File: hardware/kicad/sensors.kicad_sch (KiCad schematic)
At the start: 21 parts, among them J3 JST SM06B-GHS-TB (SEN66-SIN-T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, J4 1x5 P1.27mm through-hole head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, J7 1x8 P2.54 mm female socket (M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, J8 1x8 P2.54 mm female socket (M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

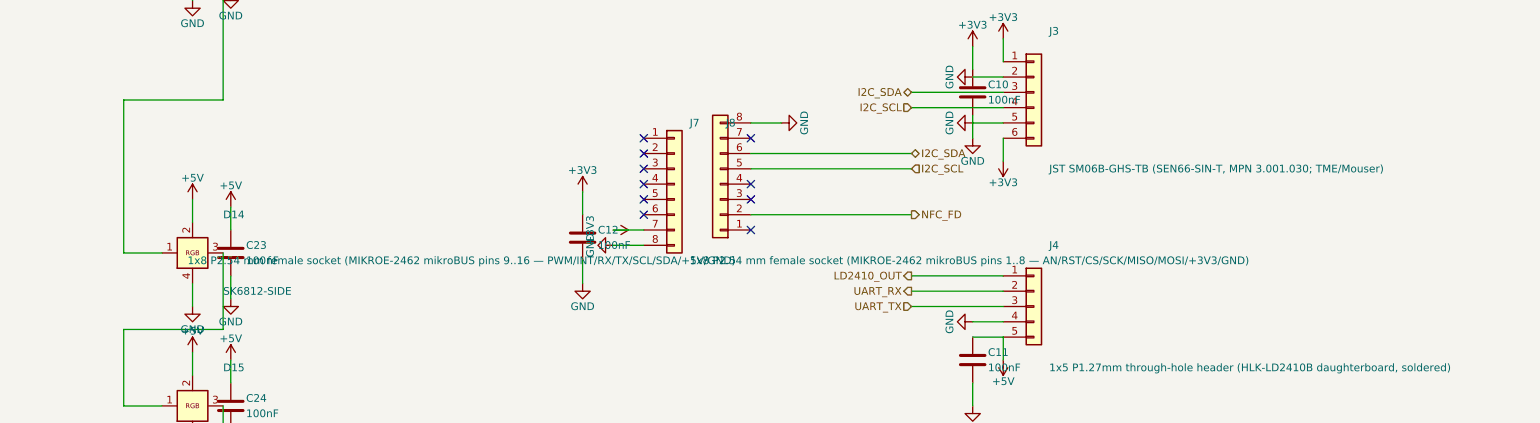
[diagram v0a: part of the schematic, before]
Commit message: hardware+firmware: remove the dynamic NFC tag (MIKROE-2462 / NT3H1101)
Closes #7.

The NFC feature is dropped entirely: RF coupling through the AK-N-94
cover is unusable as integrated, the only workable fix (cover-mounted
antenna) breaks the aesthetic pillar, and the LED ring + HA dashboard
already cover the need. Recorded in CLAUDE.md Out-of-scope.

Hardware (boardgen):
- MOD2 (oas:MIKROE-2462_Reference), J7 + J8 mikroBUS sockets and C12
  decoupling removed from schematic, placement, footprints, Z-clearance
  and the stage-18 whitelist (9 -> 8 documented customs).
- GPIO 3 (net NFC_FD) freed -> spare no_connect, same pattern as GPIO 1
  in the SW1 removal; ten spare safe-non-strap GPIOs now.
- Routing snapshot 600 seg + 40 via -> 586 seg + 43 via: /MCU/NFC_FD
  (2 seg) and 12 dead GND stitches anchored at the removed pads swept;
  3 bridge vias added where former J7.7/J8.5/J8.6 THT pads carried the
  live +3V3 / I2C_SCL / I2C_SDA layer transitions feeding the SEN66
  (J3). Clearance at the via spots >= 0.71 mm vs the 0.20 mm rule.
- I2C bus is now SEN66 + Qwiic; stage 26 rise time improves to
  278/277 ns (was 306/305) vs the 1000 ns Standard-mode ceiling.
- POWER_BUDGET, EXTERNAL_MODULES, THT_REFERENCES, tests and BOM/CPL
  deliverables updated; dead 2x8-connector schematic helper removed.

Firmware (esphome):
- packages/nfc.yaml deleted; dashboard_url substitution and all NFC
  references removed from oas.yaml, package comments and READMEs.
- HARDWARE-COMPAT-v0.51.md: removal recorded as final; the five v0.51
  boards keep unpopulated J7/J8/MOD2 footprints.

Verification: implemented and adversarially reviewed by two independent
agents; build.py 35/35 PASS on both runs; DRC 0 violations /
0 unconnected; ERC 0/0; F.Cu pour refills the former mikroBUS field
with no orphan islands; deliverables (BOM/CPL/gerbers/ibom) carry zero
NFC references.

Co-Authored-By: Claude Fable 5 <noreply@anthropic.com>
Claude-Session: https://claude.ai/code/session_017QqgHNrNySNTKB44F1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
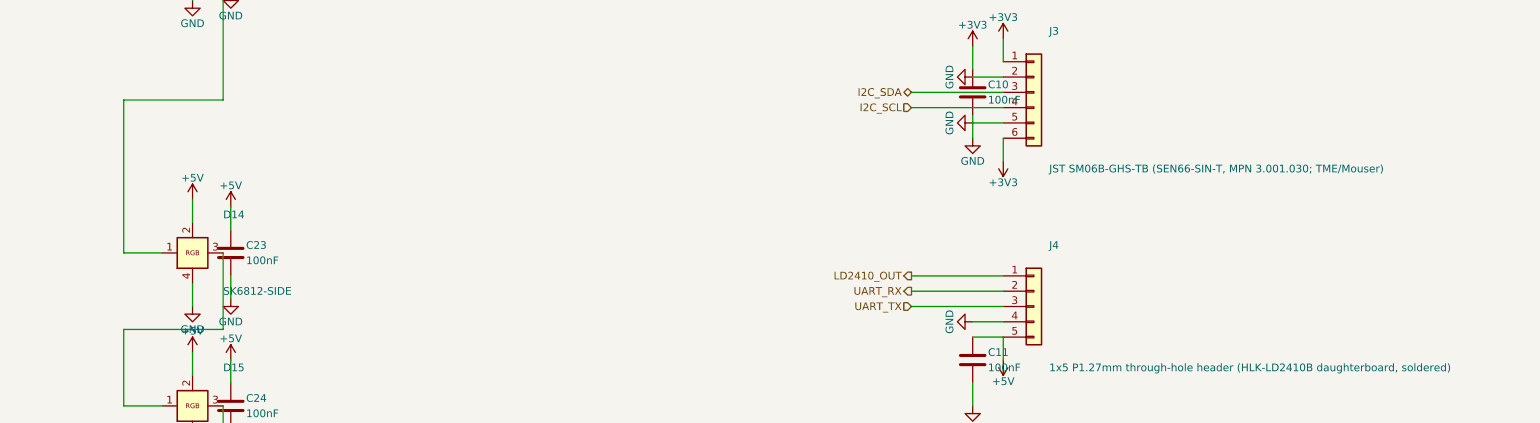
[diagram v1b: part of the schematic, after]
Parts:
- removed C12: 100nF, Capacitor_SMD:C_0603_1608Metric, symbol Device:C
- removed J7, J8: 1x8 P2.54 mm female socket (MIKROE-2462 mikroBUS 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, Connector_PinSocket_2.54mm:PinSocket_1x08_P2.54mm_Vertical, symbol Connector_Generic:Conn_01x08
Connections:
- no-connect marks 11 -> 1

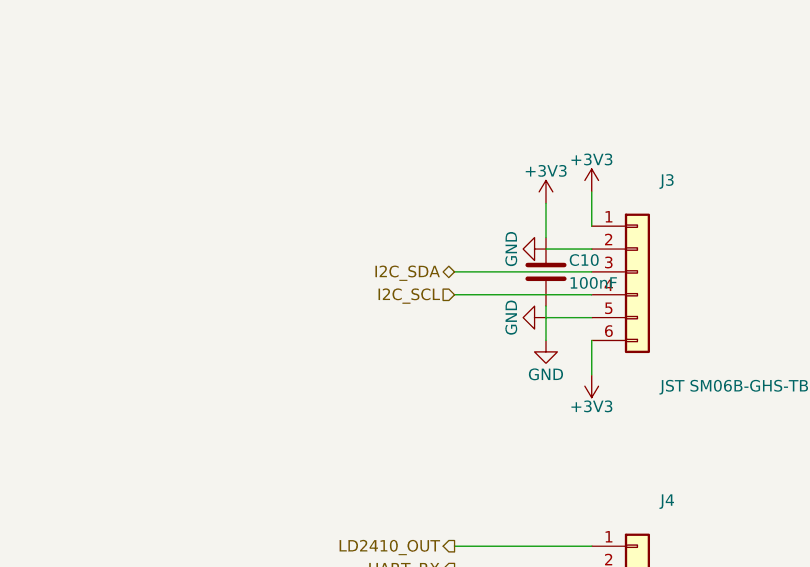
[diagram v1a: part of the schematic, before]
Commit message: hardware+firmware: mirror J3 (SEN66) pinout so a straight GH lead mates correctly
Closes #6.

Root cause (SEN6x datasheet v0.92 Table 16 p. 15 + JST GH keying): a
standard flat parallel-wire JST GH lead mirrors pin positions between
two face-to-face keyed connectors (k -> 7-k). Sensirion's pinout is
deliberately power-symmetric (1/6 VDD and 2/5 GND internally tied), so
the mirror is invisible on power and manifests only as SDA<->SCL —
exactly the v0.51 bench symptom. The host-side J3 must therefore be the
positional MIRROR of the module table; v0.51 copied it pin-for-pin.

Hardware:
- J3 pins 3/4 swapped: corrected J3 = 1=VDD, 2=GND, 3=SCL, 4=SDA,
  5=GND, 6=VDD (boardgen/_sch_sensors.py, tags j3-p3-scl / j3-p4-sda).
- Copper: the pin swap made the pre-existing west-end crossover braid
  at the two I2C bridge vias unnecessary — unwound into two direct
  via->trunk connectors (-4/+3 segments, min clearance 0.66 mm);
  corridor nets to J3 renamed. Snapshot 585 segments + 43 vias.
- New Lesson 21 in CLAUDE.md + stage 19 check E (6-pin J3 canon
  anchored to the wire tags; shared anchor scanner refactored out of
  check D, whose behavior is unchanged). Cable sourcing caveat (flat
  parallel-wire vs opposite-crimp 1:1) recorded in Lesson 21,
  HARDWARE-COMPAT and the EXTERNAL_MODULES SEN66 accessory entry.

Firmware (two hardware generations):
- oas.yaml: i2c_sda_pin/i2c_scl_pin substitutions, defaults GPIO6/GPIO7
  (= corrected board); air-quality.yaml consumes them.
- New examples/v0.51-board.yaml: per-device override (GPIO7/GPIO6) for
  the five v0.51 prototypes + !secret proxy instructions.
- HARDWARE-COMPAT-v0.51.md: flash matrix, exact override snippet, both
  -direction warnings, root cause.

Verification: implemented and adversarially reviewed by two independent
agents (reviewer independently re-derived the mirror from fresh
datasheet downloads and a connectivity model; APPROVE-WITH-NITS, all
four findings applied). build.py 35/35 PASS on three runs; DRC
0 violat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
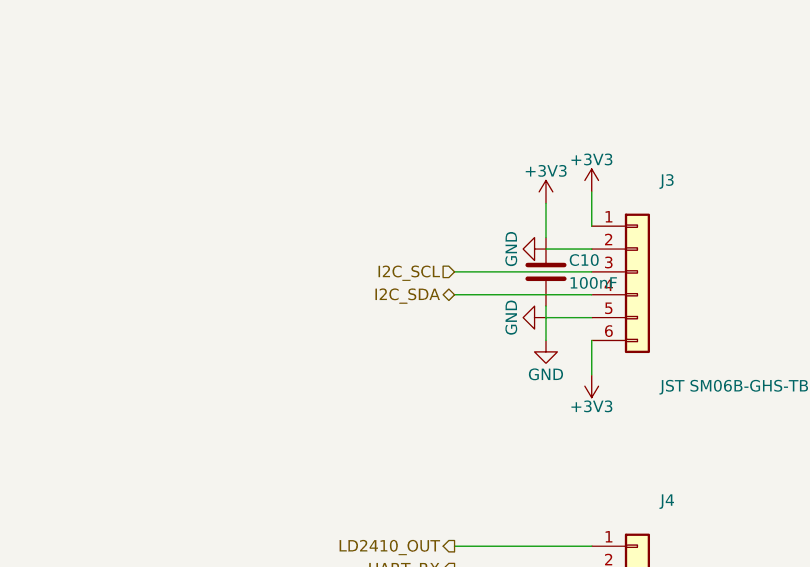
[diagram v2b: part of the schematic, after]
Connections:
- net I2C_SCL: now also J3.3 (Pin_3); no longer J3.4 (Pin_4)
- net I2C_SDA: now also J3.4 (Pin_4); no longer J3.3 (Pin_3)
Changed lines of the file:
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@@
 	)
 )
-(hierarchical_label "I2C_SDA"
-	(shape bidirectional)
+(hierarchical_label "I2C_SCL"
+	(shape input)
 	(at 160.02 110.49 180)
 	(effects
@@
 	)
 )
-(hierarchical_label "I2C_SCL"
-	(shape input)
+(hierarchical_label "I2C_SDA"
+	(shape bidirectional)
 	(at 160.02 113.03 180)
 	(effects

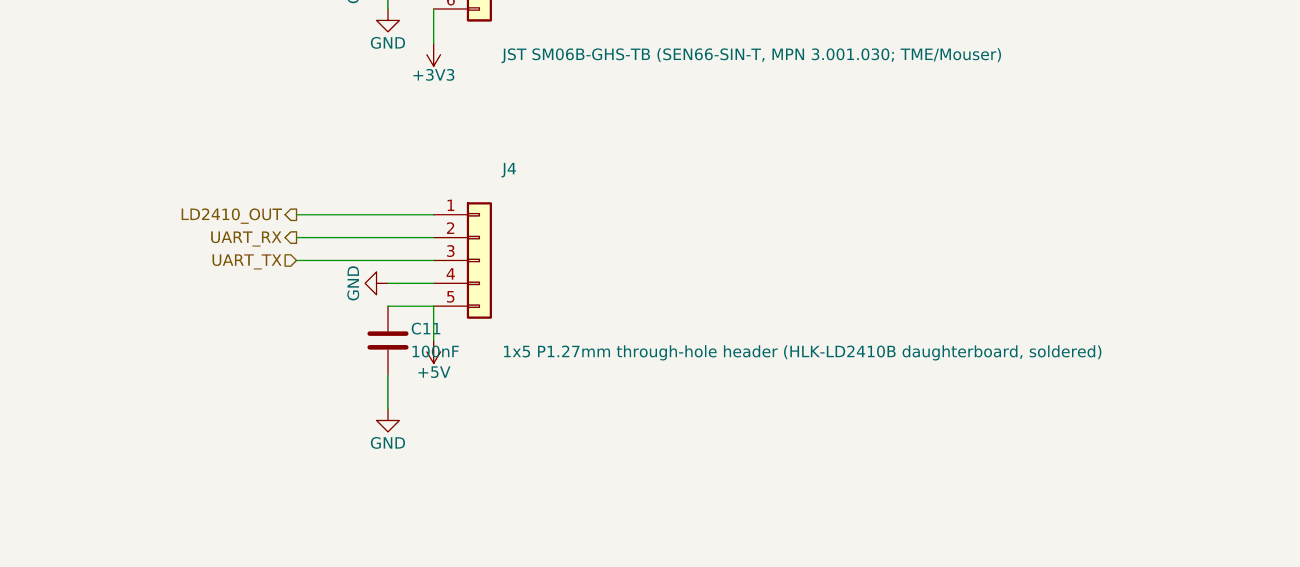
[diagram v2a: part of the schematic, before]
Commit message: hardware: rework J4 for the HLK-LD2410C (2.54 mm header) — issue #9
Two HLK-LD2410B samples from different sellers, both on firmware build
2.44.25070917, showed the same fault on the v0.51 prototype: radar alive
(OUT tracks presence, BLE works) but the UART totally mute. The board was
exonerated at every layer with a standalone ESP-IDF test firmware (no
ESPHome): supply present, J4 joints electrically connected, no bridges,
both pin mappings, three baud rates, direct protocol commands and a
factory reset — silence throughout. Independent of that, the -B's 5-pad
1.27 mm castellated edge has burned this project twice on hand-soldering.

The LD2410C is the same radar with the same UART protocol at 256000 baud
(unchanged ESPHome `ld2410` component), on a 22 x 16 mm board with five
plated holes at 2.54 mm pitch — an ordinary gold-pin header.

Board side:
- J4 becomes stock Connector_PinHeader_2.54mm:PinHeader_1x05_P2.54mm_
  Vertical, emitted verbatim through the parse-and-emit path (Lesson 1/2).
- Pad 1 at PCB (-37.00, +12.00), row running east; module body 22 x 16 mm
  at X -42.92..-20.92, Y +10.58..+26.58. Position is fixed between H2 to
  the west and the LED ring to the east — the only 22 mm slot on the
  board, and east/south of the old -B strip.
- Pin order per the owner's orientation spec, confirmed against the
  LD2410C manual V1.00 Table 1: with the antenna face toward the viewer
  and the pin row north (i.e. the PCB top view), pins run TX, RX, OUT,
  GND, VCC from west to east. This is the MIRROR of the -B order. Net
  binding keeps the MCU-centric crossover: module Tx -> UART_RX (GPIO 17),
  module Rx -> UART_TX (GPIO 16), OUT -> GPIO 2.
- Body anchor is DERIVED from the J4 datum, never authored — the Lesson 22
  corollary — and a test re-derives it.
- Silk: five per-hole labels reading "J4 TX RX OUT GND VCC" north of the
  row (south would sit under the module), body outline with the north edge
  broken into corner stubs to clear the header's own silk frame,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
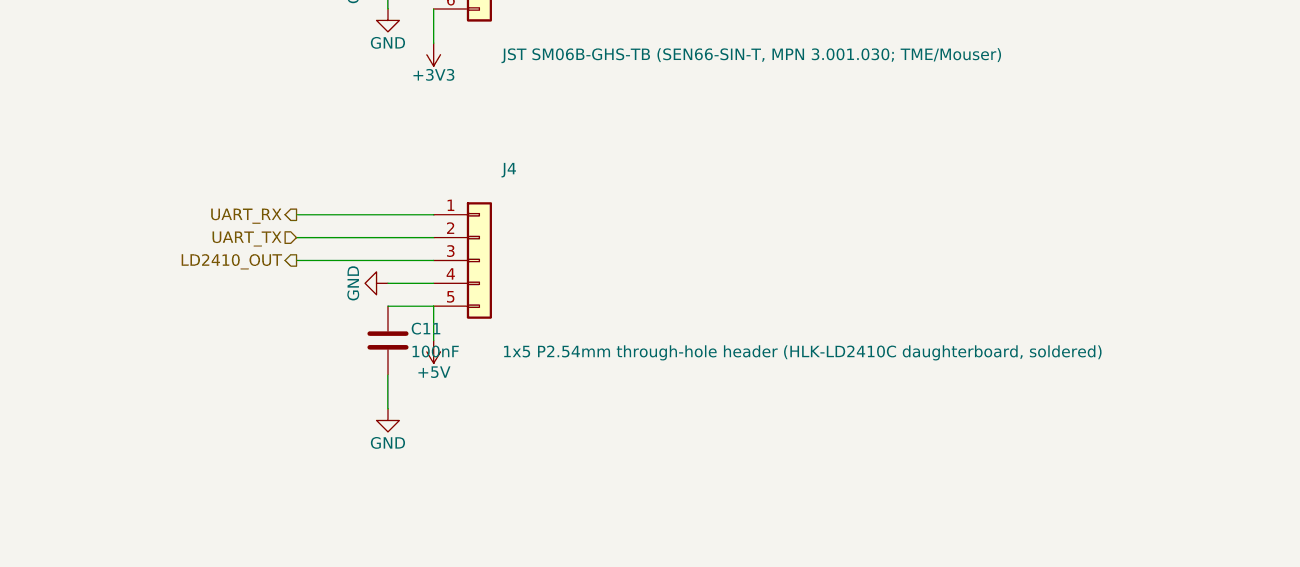
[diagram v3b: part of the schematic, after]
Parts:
- J4: value 1x5 P1.27mm through-hole header (HLK-LD2410B daughterboard, soldered) -> 1x5 P2.54mm through-hole header (HLK-LD2410C daughterboard, soldered); footprint Connector_PinHeader_1.27mm:PinHeader_1x05_P1.27mm_Vertical -> Connector_PinHeader_2.54mm:PinHeader_1x05_P2.54mm_Vertical
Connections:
- net LD2410_OUT: now also J4.3 (Pin_3); no longer J4.1 (Pin_1)
- net UART_RX: now also J4.1 (Pin_1); no longer J4.2 (Pin_2)
- net UART_TX: now also J4.2 (Pin_2); no longer J4.3 (Pin_3)
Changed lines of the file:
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@@
 	)
 )
-(hierarchical_label "LD2410_OUT"
+(hierarchical_label "UART_RX"
 	(shape output)
 	(at 160.02 140.97 180)
@@
 	)
 )
-(hierarchical_label "UART_RX"
-	(shape output)
+(hierarchical_label "UART_TX"
+	(shape input)
 	(at 160.02 143.51 180)
 	(effects
@@
 	)
 )
-(hierarchical_label "UART_TX"
-	(shape input)
+(hierarchical_label "LD2410_OUT"
+	(shape output)
 	(at 160.02 146.05 180)
 	(effects
@@
         			)
         		)
-        		(property "Value" "1x5 P1.27mm through-hole header (HLK-LD2410B daughterboard, soldered)"
+        		(property "Value" "1x5 P2.54mm through-hole header (HLK-LD2410C daughterboard, soldered)"
         			(at 182.88 156.21 0)
         			(effects
@@
         			)
         		)
-        		(property "Footprint" "Connector_PinHeader_1.27mm:PinHeader_1x05_P1.27mm_Vertical"
+        		(property "Footprint" "Connector_PinHeader_2.54mm:PinHeader_1x05_P2.54mm_Vertical"
         			(at 180.34 146.05 0)
         			(effects

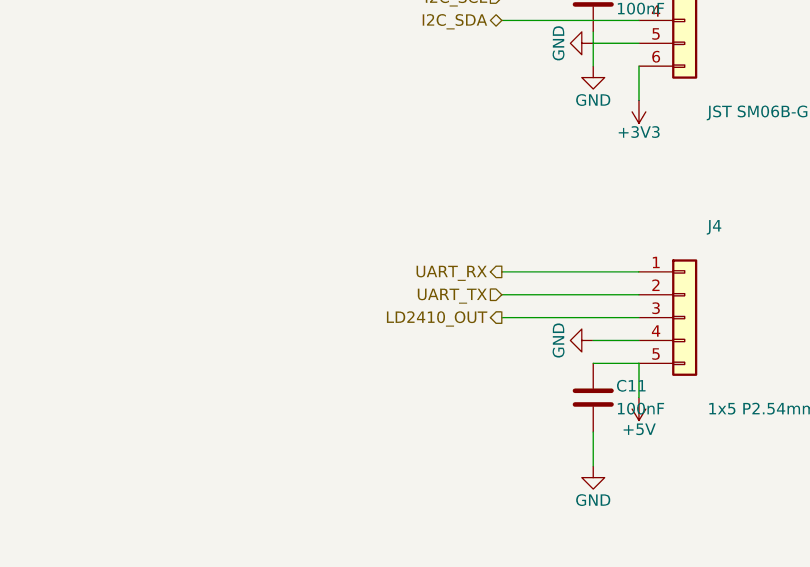
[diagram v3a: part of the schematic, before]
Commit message: hardware+firmware: move the LD2410 UART off GPIO16/17 (CP2102N contention)
The LD2410 UART sat on GPIO16/17 from v0.4 on the reasoning that those are
"just the default UART0 pins" and the C6's GPIO matrix can re-route UART0.
That reasoning covers the SoC only. On the ESP32-C6-DevKitM-1 the same two
pads are wired through populated 0 R links (R9 -> CP2102N RXD pin 25,
R7 -> CP2102N TXD pin 26) to the onboard USB-UART bridge, and that bridge's
VDD (6) + REGIN (7) tie to VCC_3V3 -- the board rail OAS drives at J5.1 --
not to USB VBUS (pin 8 only sees the R19/R18 sense divider). So the bridge
is powered whenever the unit is, and its TXD is a push-pull output parked
on the ESP's RX net. Two drivers, one node.

Bench-proved on a v0.51 board with the radar unpowered (24 V off) and the
bridge's own USB port empty, probing with the ESP's internal pulls:
  GPIO2  pu=1/pd=0  FLOATING
  GPIO16 pu=1/pd=0  FLOATING
  GPIO17 pu=1/pd=1  DRIVEN
The two control pins follow the pulls; GPIO17 holds HIGH against its own
pull-down with nothing on that net but the bridge's TXD.

Fix: the pair moves to GPIO 1 (TX) / GPIO 0 (RX) -- free, adjacent,
non-strap pads on J5, the socket row nearest J4. Nets renamed
LD2410_UART_TX / LD2410_UART_RX; UART_TX / UART_RX stay as the true console
on GPIO16/17, reaching only the DNP recovery header J2 (that header exists
to serial-flash a module whose USB ports are dead, so it belongs on the ROM
bootloader's own pins and must not follow a peripheral around).

GPIO16/17 move into GPIO_RESERVED, and stage 06 grows a console-pin check
that fails if any refdes other than J6/J2 appears on either console net --
a dict entry is a comment, a check is a guarantee.

Replacement pins vetted the same way the old ones failed: GPIO0/1 double as
XTAL_32K_P/N and the DevKitM-1 does carry that network, but Y1, C4/C5 and
R1 are all (NC) on the Espressif schematic and only the 0 R links R3/R2 to
the header are populated -- the pads are electrically bare.

Firmware gains ld2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
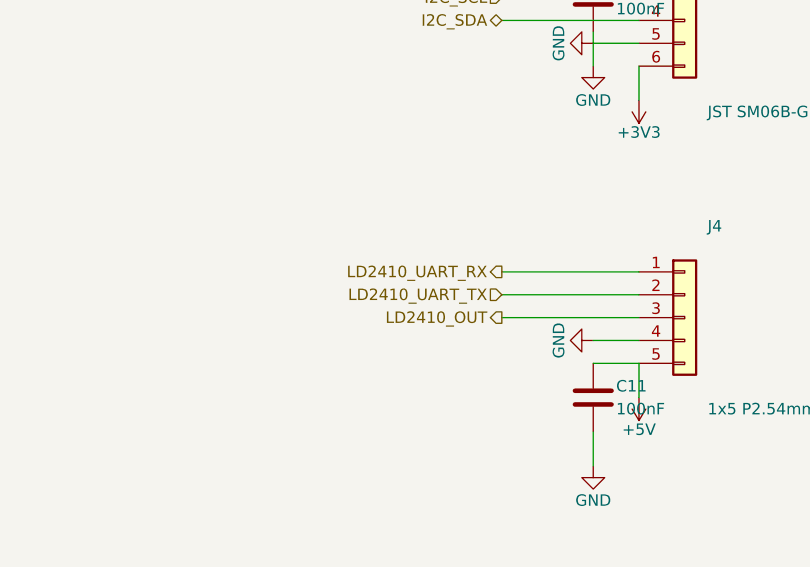
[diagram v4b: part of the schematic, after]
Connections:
- net UART_RX renamed LD2410_UART_RX
- net UART_TX renamed LD2410_UART_TX
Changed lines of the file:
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@@
 	)
 )
-(hierarchical_label "UART_RX"
+(hierarchical_label "LD2410_UART_RX"
 	(shape output)
 	(at 160.02 140.97 180)
@@
 	)
 )
-(hierarchical_label "UART_TX"
+(hierarchical_label "LD2410_UART_TX"
 	(shape input)
 	(at 160.02 143.51 180)
